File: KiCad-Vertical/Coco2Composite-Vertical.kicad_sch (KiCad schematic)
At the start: 17 parts, among them J1 TO_COCO2, J2 AUDIO_JACK_3.5MM_KIT, Q1 PN2907, Q2 2N2222, U1 MC1372

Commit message: Updated the vertical model to let the resistors lie down on the board, kept the old one in case someone wants the board the same way it was
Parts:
- R1, R4, R5, R6, R7: footprint Resistor_THT:R_Axial_DIN0204_L3.6mm_D1.6mm_P2.54mm_Vertical -> Resistor_THT:R_Axial_DIN0204_L3.6mm_D1.6mm_P5.08mm_Horizontal
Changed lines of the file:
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@@
 			)
 		)
-		(property "Footprint" "Resistor_THT:R_Axial_DIN0204_L3.6mm_D1.6mm_P2.54mm_Vertical"
+		(property "Footprint" "Resistor_THT:R_Axial_DIN0204_L3.6mm_D1.6mm_P5.08mm_Horizontal"
 			(at 200.66 121.92 0)
 			(effects
@@
 			)
 		)
-		(property "Footprint" "Resistor_THT:R_Axial_DIN0204_L3.6mm_D1.6mm_P2.54mm_Vertical"
+		(property "Footprint" "Resistor_THT:R_Axial_DIN0204_L3.6mm_D1.6mm_P5.08mm_Horizontal"
 			(at 134.62 58.42 0)
 			(effects
@@
 			)
 		)
-		(property "Footprint" "Resistor_THT:R_Axial_DIN0204_L3.6mm_D1.6mm_P2.54mm_Vertical"
+		(property "Footprint" "Resistor_THT:R_Axial_DIN0204_L3.6mm_D1.6mm_P5.08mm_Horizontal"
 			(at 238.76 121.92 0)
 			(effects
@@
 			)
 		)
-		(property "Footprint" "Resistor_THT:R_Axial_DIN0204_L3.6mm_D1.6mm_P2.54mm_Vertical"
+		(property "Footprint" "Resistor_THT:R_Axial_DIN0204_L3.6mm_D1.6mm_P5.08mm_Horizontal"
 			(at 220.98 114.3 0)
 			(effects
@@
 			)
 		)
-		(property "Footprint" "Resistor_THT:R_Axial_DIN0204_L3.6mm_D1.6mm_P2.54mm_Vertical"
+		(property "Footprint" "Resistor_THT:R_Axial_DIN0204_L3.6mm_D1.6mm_P5.08mm_Horizontal"
 			(at 185.42 114.3 0)
 			(effects

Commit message: Increased the footprint for the resistors since the one I picked was still too small
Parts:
- R1, R4, R5, R6, R7: footprint Resistor_THT:R_Axial_DIN0204_L3.6mm_D1.6mm_P5.08mm_Horizontal -> Resistor_THT:R_Axial_DIN0207_L6.3mm_D2.5mm_P7.62mm_Horizontal
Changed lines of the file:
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@@
 			)
 		)
-		(property "Footprint" "Resistor_THT:R_Axial_DIN0204_L3.6mm_D1.6mm_P5.08mm_Horizontal"
+		(property "Footprint" "Resistor_THT:R_Axial_DIN0207_L6.3mm_D2.5mm_P7.62mm_Horizontal"
 			(at 200.66 121.92 0)
 			(effects
@@
 			)
 		)
-		(property "Footprint" "Resistor_THT:R_Axial_DIN0204_L3.6mm_D1.6mm_P5.08mm_Horizontal"
+		(property "Footprint" "Resistor_THT:R_Axial_DIN0207_L6.3mm_D2.5mm_P7.62mm_Horizontal"
 			(at 134.62 58.42 0)
 			(effects
@@
 			)
 		)
-		(property "Footprint" "Resistor_THT:R_Axial_DIN0204_L3.6mm_D1.6mm_P5.08mm_Horizontal"
+		(property "Footprint" "Resistor_THT:R_Axial_DIN0207_L6.3mm_D2.5mm_P7.62mm_Horizontal"
 			(at 238.76 121.92 0)
 			(effects
@@
 			)
 		)
-		(property "Footprint" "Resistor_THT:R_Axial_DIN0204_L3.6mm_D1.6mm_P5.08mm_Horizontal"
+		(property "Footprint" "Resistor_THT:R_Axial_DIN0207_L6.3mm_D2.5mm_P7.62mm_Horizontal"
 			(at 220.98 114.3 0)
 			(effects
@@
 			)
 		)
-		(property "Footprint" "Resistor_THT:R_Axial_DIN0204_L3.6mm_D1.6mm_P5.08mm_Horizontal"
+		(property "Footprint" "Resistor_THT:R_Axial_DIN0207_L6.3mm_D2.5mm_P7.62mm_Horizontal"
 			(at 185.42 114.3 0)
 			(effects

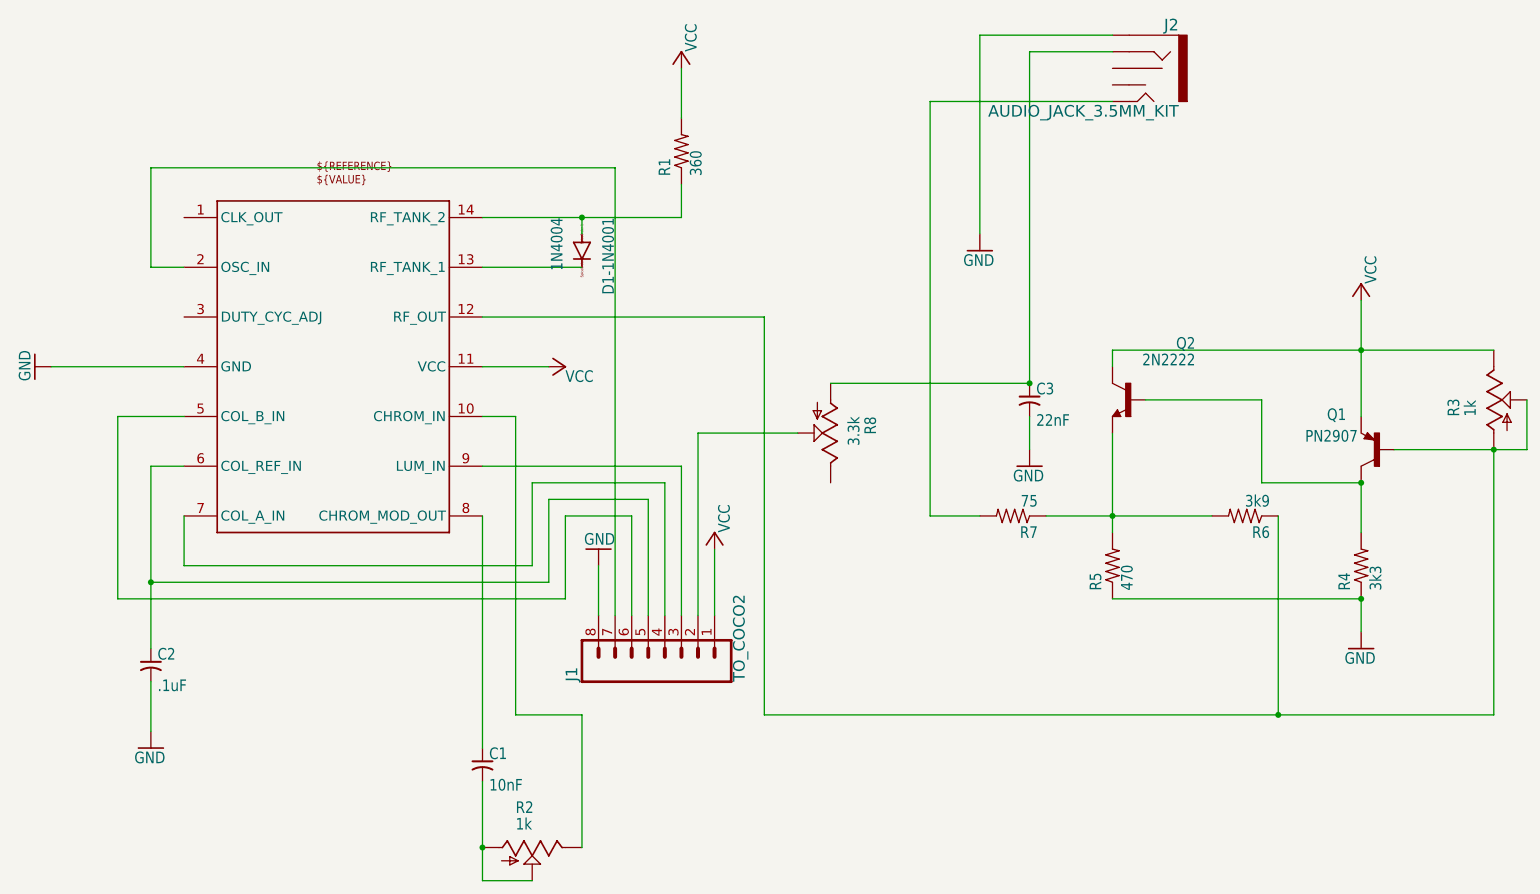
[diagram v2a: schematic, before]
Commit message: Overhauled vertical board based on lessons learned working on horizontal board
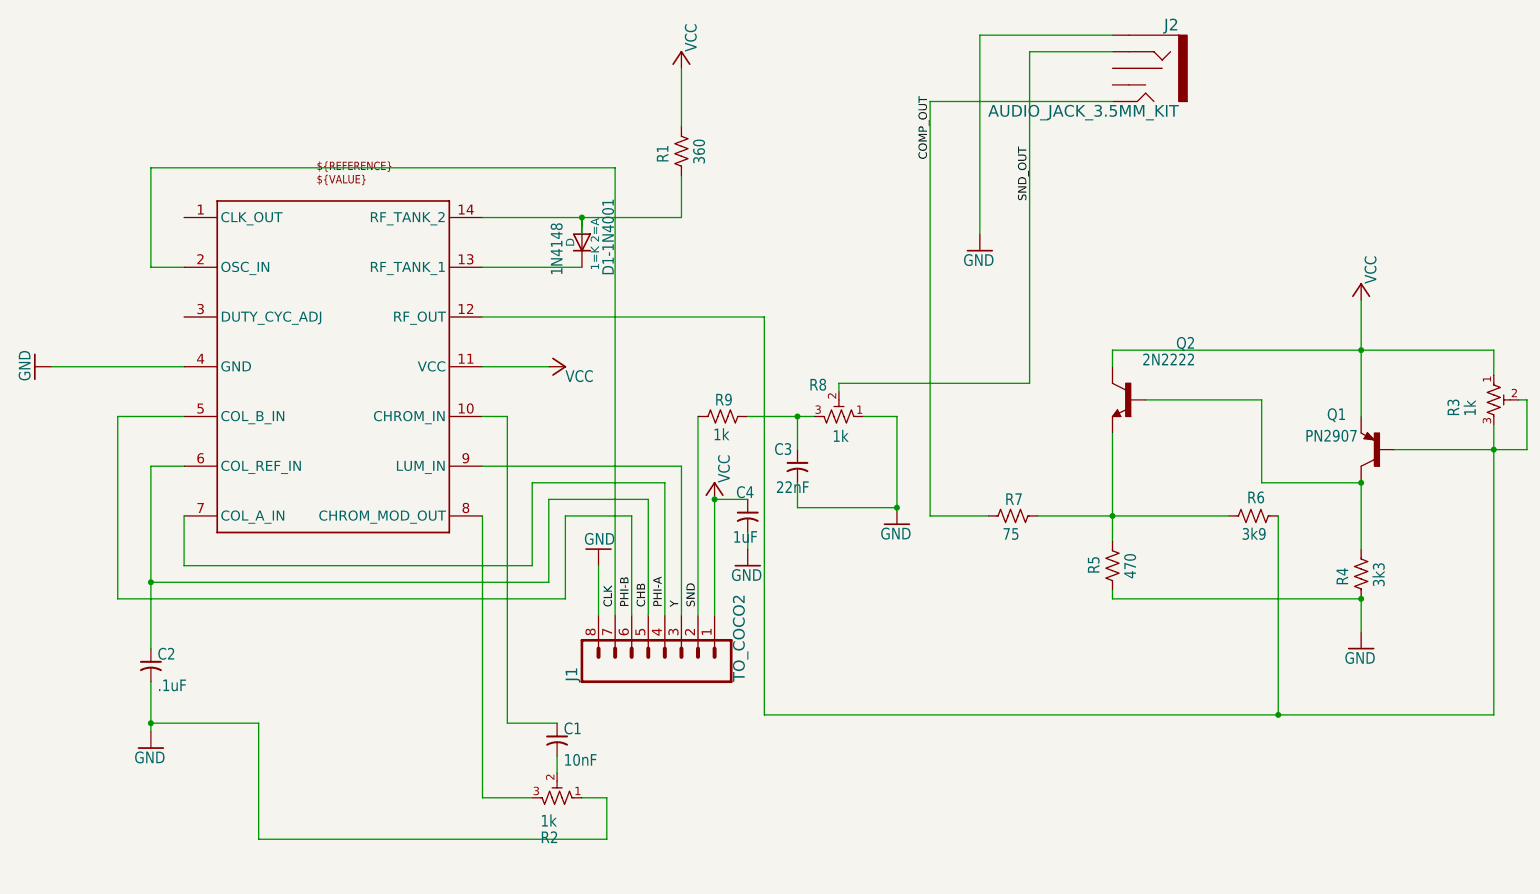
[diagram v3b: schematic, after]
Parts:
- added C4: 1uF, Capacitor_THT:C_Disc_D3.0mm_W2.0mm_P2.50mm, symbol Device:C_Small_US
- added R9: 1k, Resistor_THT:R_Axial_DIN0207_L6.3mm_D2.5mm_P7.62mm_Horizontal, symbol Device:R_US
- D1-1N4001: value 1N4004 -> 1N4148; footprint Diode_THT:D_DO-41_SOD81_P10.16mm_Horizontal -> Diode_THT:D_DO-35_SOD27_P7.62mm_Horizontal; symbol Coco2Composite-eagle-import:1N4004 -> Diode:1N4148
- R1, R4, R5, R6, R7: symbol Coco2Composite-eagle-import:R-US_0204/2V -> Device:R_US
- R2, R3: symbol Coco2Composite-eagle-import:TRIM_US-B25U -> Device:R_Potentiometer_Trim_US
- R8: value 3.3k -> 1k; symbol Coco2Composite-eagle-import:TRIM_US-B25U -> Device:R_Potentiometer_Trim_US
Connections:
- net GND: now also R2.1, R4.2, R5.2, R8.1, C4.2; no longer R4.1, R5.1
- net VCC: now also R1.1, R3.1, C4.1; no longer R1.2, R3.E
- net at Q1.C, Q2.2 (B): now also R4.1; no longer R4.2
- net SND: now reaches J1.2
- net SND: now also R9.1; no longer R8.S
- net at U1.10 (CHROM_IN): now also C1.1; no longer R2.E
- net at U1.13 (RF_TANK_1): now also D1-1N4001.1 (K); no longer D1-1N4001.C
- net Y: now reaches J1.3, U1.9 (LUM_IN)
- net PHI-A: now reaches J1.4, U1.7 (COL_A_IN)
- net CHB: now reaches C2.1, J1.5, U1.6 (COL_REF_IN)
- net PHI-B: now reaches J1.6, U1.5 (COL_B_IN)
- net CLK: now reaches J1.7, U1.2 (OSC_IN)
- net at R7.2: now also Q2.1 (E), R5.1, R6.1; no longer J2.TIP
- net at U1.8 (CHROM_MOD_OUT): now also R2.3; no longer C1.1
- new net: C3.1, R8.3, R9.2
- new net: C1.2, R2.2
- new net: D1-1N4001.2 (A), R1.2, U1.14 (RF_TANK_2)
- new net: Q1.B, R3.2, R3.3, R6.2, U1.12 (RF_OUT)
- new net COMP_OUT: J2.TIP, R7.1
- new net SND_OUT: J2.RING, R8.2
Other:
- moved on the sheet: C1, C3

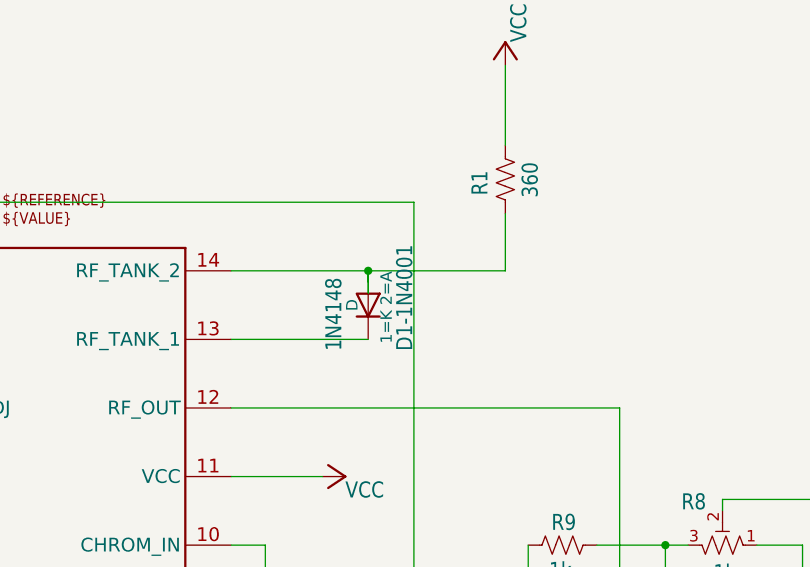
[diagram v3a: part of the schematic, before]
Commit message: Fixed label on diode
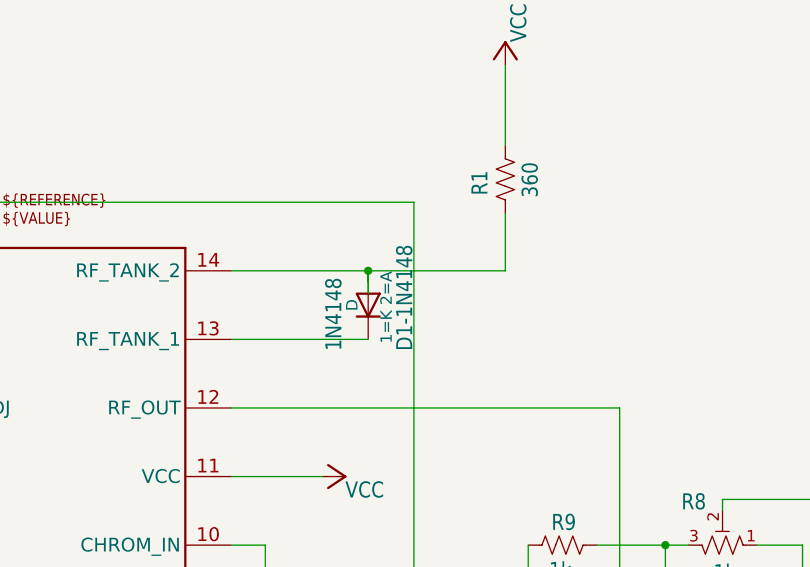
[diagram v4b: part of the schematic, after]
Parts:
- renumbered D1-1N4001 to D1-1N4148
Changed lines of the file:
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@@
 		(on_board yes)
 		(dnp no)
-		(property "Reference" "D1-1N4001"
+		(property "Reference" "D1-1N4148"
 			(at 122.4026 77.47 0)
 			(effects
@@
 			(project ""
 				(path "/59fedd81-dfb5-41c3-969a-5c6cb0470a9a"
-					(reference "D1-1N4001")
+					(reference "D1-1N4148")
 					(unit 1)
 				)

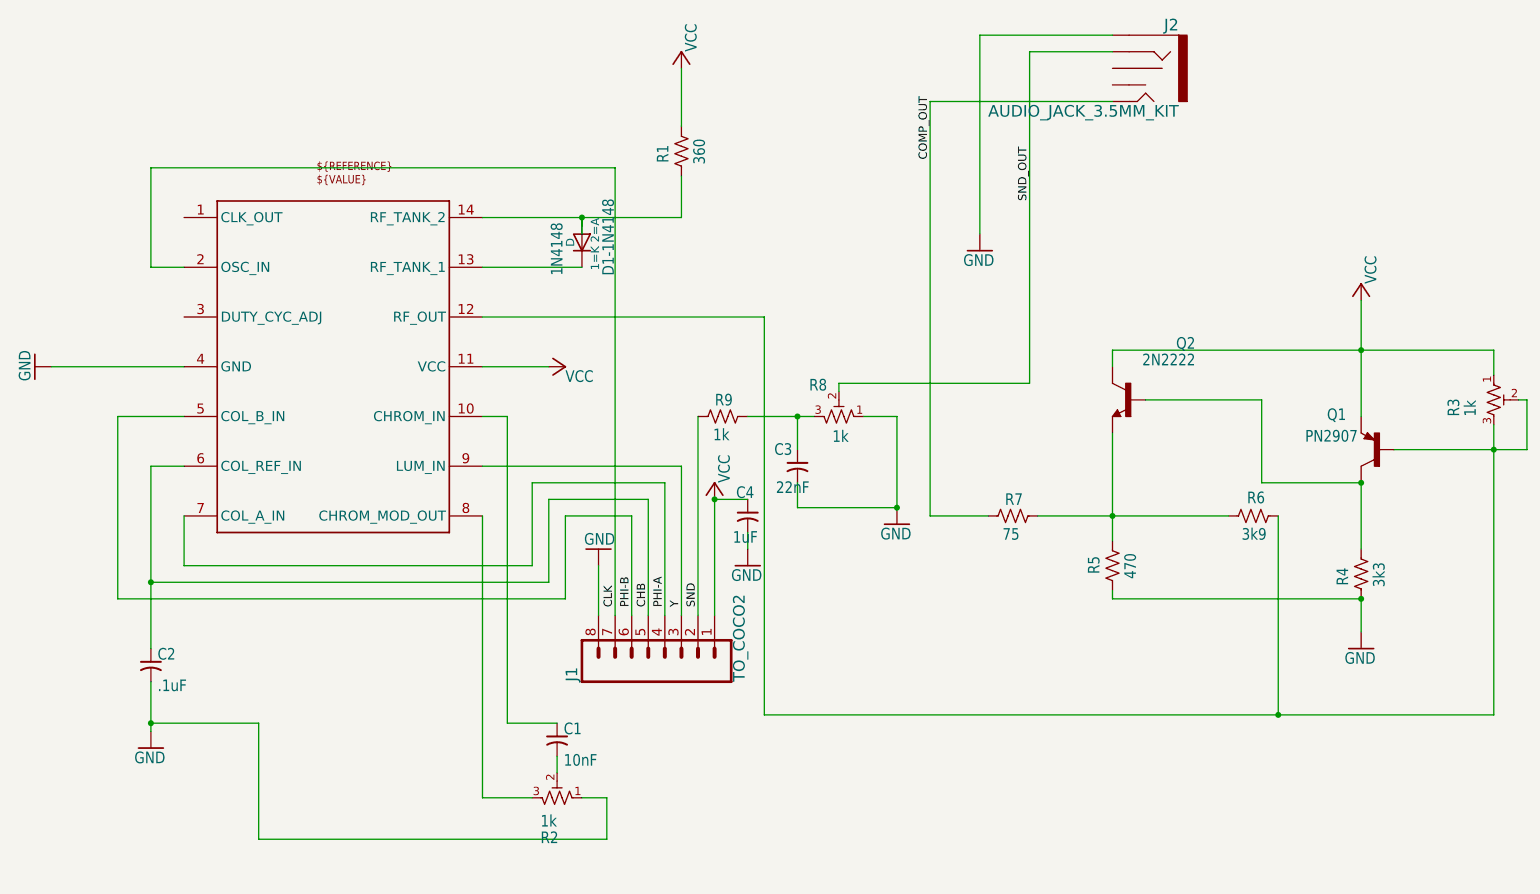
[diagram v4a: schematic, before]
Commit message: Updated some schematic symbols and rerouted a few things on the vertical board
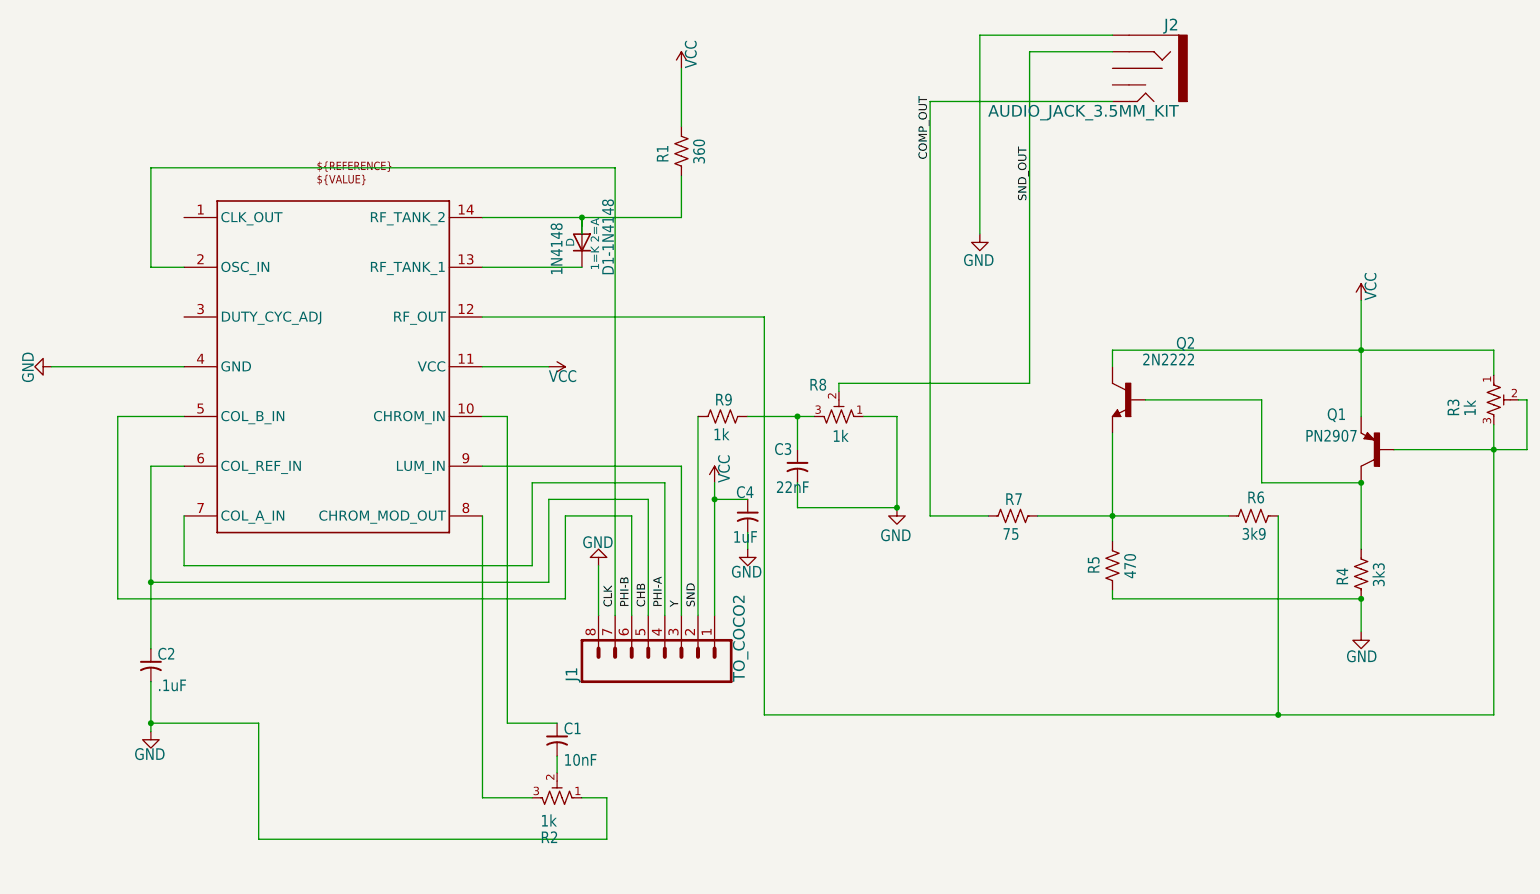
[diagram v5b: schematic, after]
